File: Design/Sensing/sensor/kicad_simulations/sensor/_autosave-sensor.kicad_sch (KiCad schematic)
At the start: 44 parts, among them J1 Conn_02x14_Counter_Clockwise, J10 Conn_01x02_Pin, J11 Conn_01x01_Pin, J12 Conn_01x02_Pin, J13 Conn_01x02_Pin, J14 Conn_01x02_Pin, J15 Conn_01x02_Pin, J16 Conn_01x01_Pin, J17 Conn_01x02_Pin, J18 Conn_01x01_Pin, J3 Conn_01x02_Pin, J4 Conn_01x02_Pin, J5 Conn_01x02_Pin, J6 Conn_01x01_Pin, J7 Conn_01x02_Pin, J8 Conn_01x02_Pin, J9 Conn_01x02_Pin, Q1 MMBT2222A, Q2 MMBT2222A, Q3 MMBT2222A, U1 TSSP58038, U2 TSSP58038, U3 TSSP58038, U4 BUF602xD, U5 BUF602xD, U6 BUF602xD

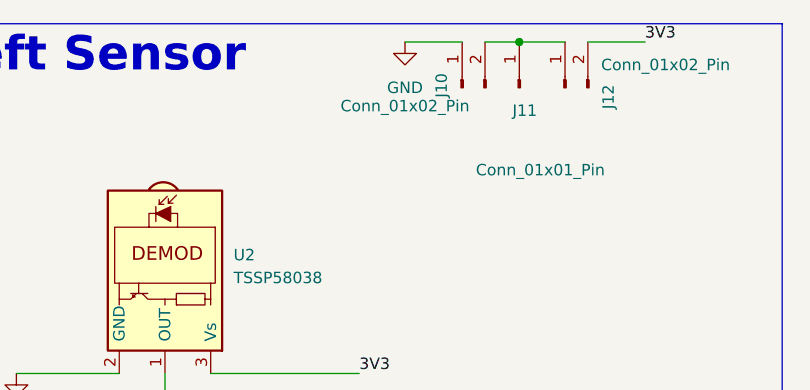
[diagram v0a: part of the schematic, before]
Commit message: PCB track done but still have 23 unrouted
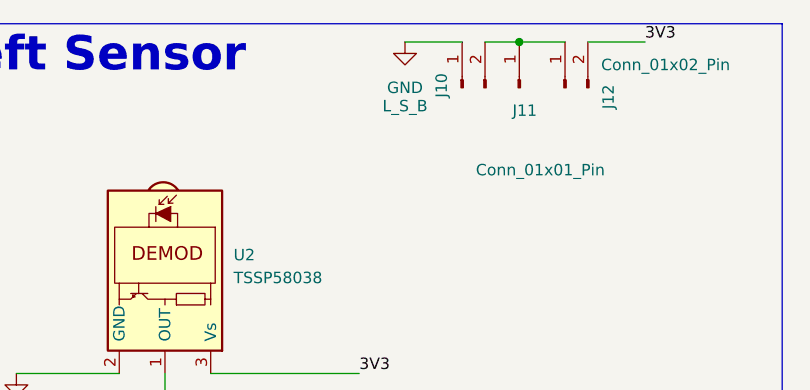
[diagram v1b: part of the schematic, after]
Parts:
- J10: value Conn_01x02_Pin -> L_S_B
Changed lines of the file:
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@@
 			)
 		)
-		(property "Value" "Conn_01x02_Pin"
+		(property "Value" "L_S_B"
 			(at 123.19 29.972 90)
 			(effects
@@
 		(on_board yes)
 		(dnp no)
-		(fields_autoplaced yes)
 		(property "Reference" "Q2"
 			(at 214.63 64.7699 0)
